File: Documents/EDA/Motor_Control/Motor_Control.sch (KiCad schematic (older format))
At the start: 7 parts

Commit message: PCB first pass
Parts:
- removed U?: ESP32-WROOM-32, RF_Module:ESP32-WROOM-32, symbol RF_Module:ESP32-WROOM-32
- added A3: Adafruit_Feather_HUZZAH32_ESP32, Module:Adafruit_Feather, symbol MCU_Module:Adafruit_Feather_HUZZAH32_ESP32
- added J1: V_MOTOR, TerminalBlock_Phoenix:TerminalBlock_Phoenix_MKDS-1,5-2_1x02_P5.00mm_Horizontal, symbol Connector:Screw_Terminal_01x02
- A1: renamed from A?; value Pololu_Breakout_DRV8825 -> R Motor Driver
- A2: renamed from A?; value Pololu_Breakout_DRV8825 -> Z Motor Driver
- C1, C2: renamed from C?; value CP -> 100u; footprint (none) -> Capacitor_THT:CP_Radial_D8.0mm_P3.50mm; symbol Device:CP -> Motor_Control-rescue:CP-Device
- M1: renamed from M?; value Stepper_Motor_bipolar -> R; footprint (none) -> Connector_PinSocket_2.54mm:PinSocket_1x04_P2.54mm_Vertical
- M2: renamed from M?; value Stepper_Motor_bipolar -> Z; footprint (none) -> Connector_PinSocket_2.54mm:PinSocket_1x04_P2.54mm_Vertical
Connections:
- net labels added: GNDD
- wire segments 68 -> 70
- no-connect marks 4 -> 25
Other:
- moved on the sheet: A1, A2, M1, M2

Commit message: libs and pcb and bom
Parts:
- removed A3: Adafruit_Feather_HUZZAH32_ESP32, Module:Adafruit_Feather, symbol MCU_Module:Adafruit_Feather_HUZZAH32_ESP32
- added J2: Barrel_Jack, Connector_BarrelJack:BarrelJack_Horizontal, symbol Connector:Barrel_Jack
- added U1: ESP32-DEVKITC-32D, MODULE_ESP32-DEVKITC-32D:MODULE_ESP32-DEVKITC-32D, symbol ESP32-DEVKITC-32D:ESP32-DEVKITC-32D
- M1, M2: footprint Connector_PinSocket_2.54mm:PinSocket_1x04_P2.54mm_Vertical -> (none)
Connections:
- net +3V3: now also U1.1 (3V3)
- net +VDC: now also J2.1
- net GND: now also J2.2
- net GNDD: now also U1.14 (GND1), U1.20 (GND3), U1.26 (GND2)
- net R_DIR: now also U1.28 (IO18)
- net R_STEP: now also U1.27 (IO19)
- net Z_DIR: now also U1.22 (IO22)
- net Z_STEP: now also U1.21 (IO23)
- no-connect marks 25 -> 4
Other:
- moved on the sheet: A1, A2, C1, C2, J1, M1, M2

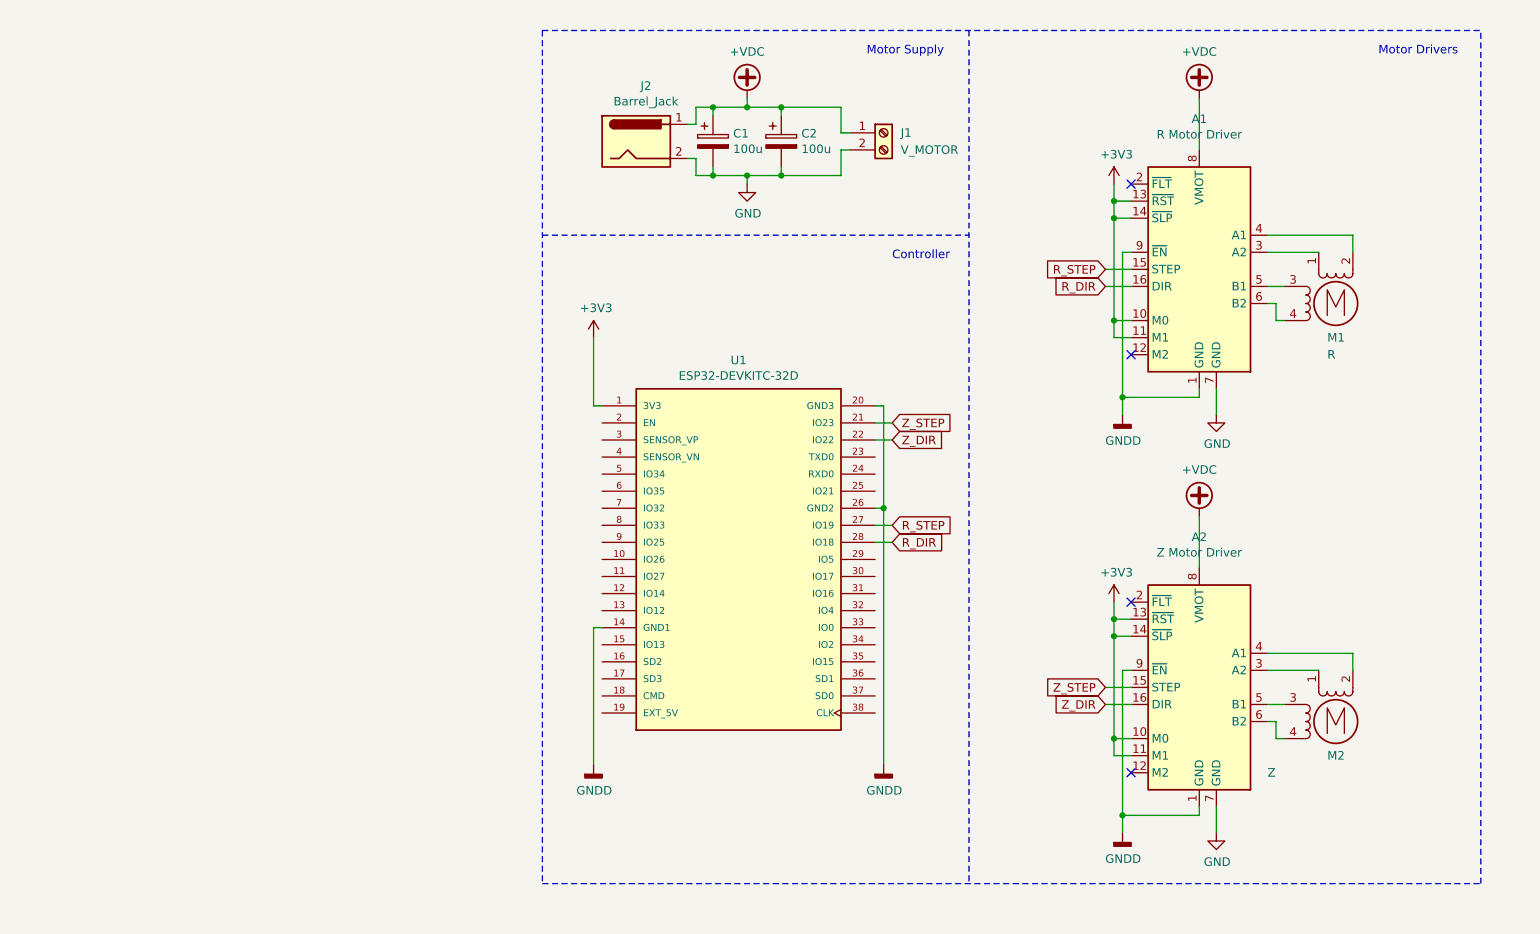
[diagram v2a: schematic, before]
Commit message: connectors placed
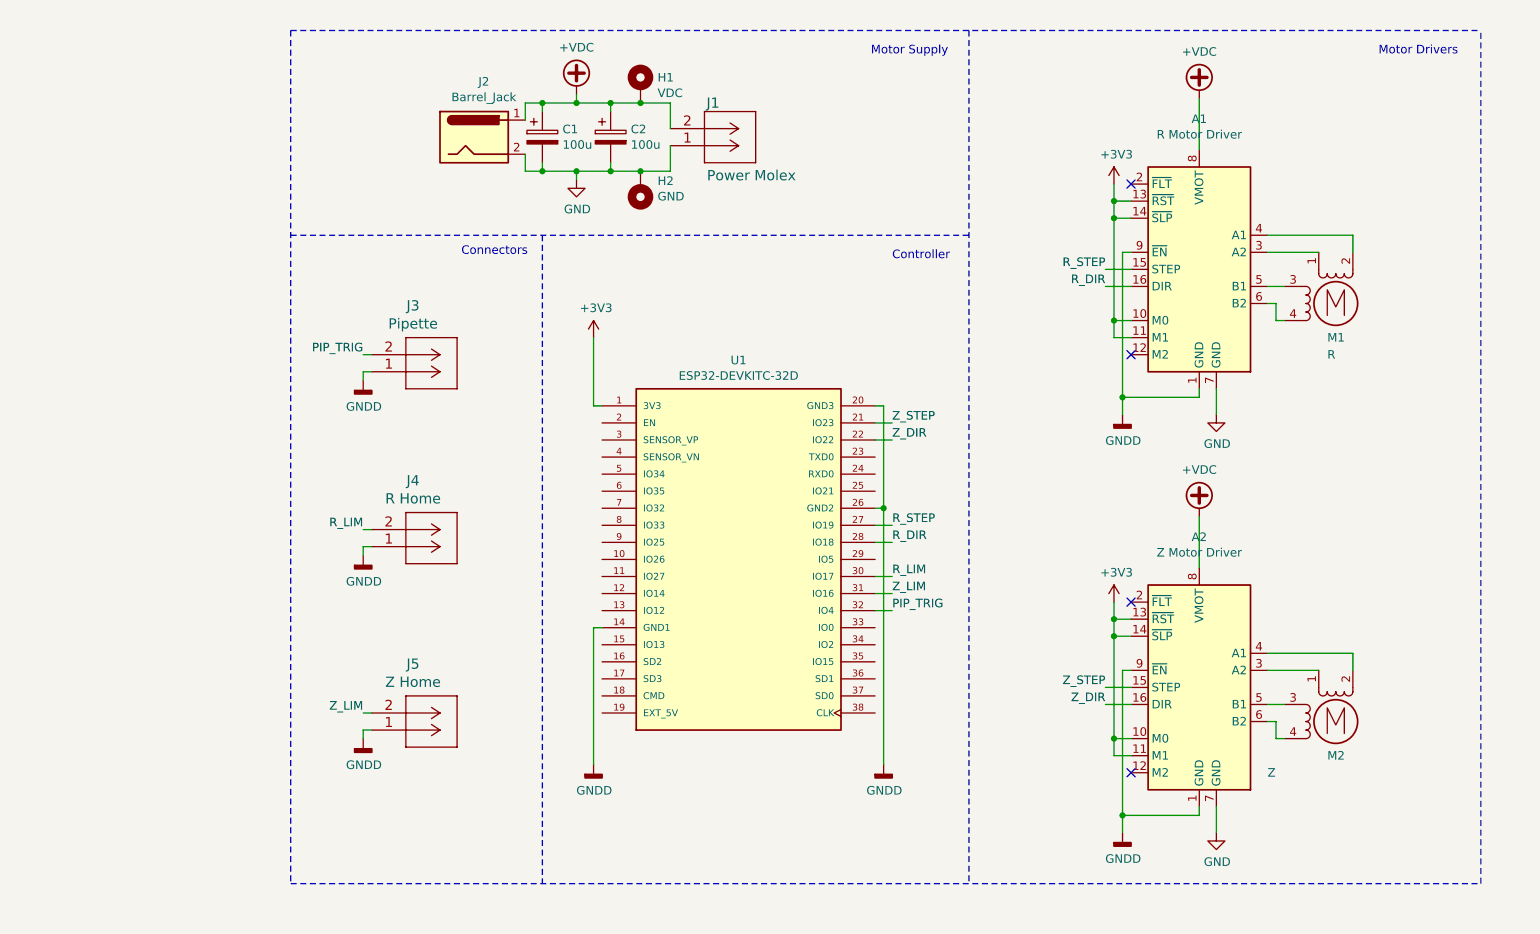
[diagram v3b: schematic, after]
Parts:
- removed J1: V_MOTOR, TerminalBlock_Phoenix:TerminalBlock_Phoenix_MKDS-1,5-2_1x02_P5.00mm_Horizontal, symbol Connector:Screw_Terminal_01x02
- added H1: VDC, MountingHole:MountingHole_3.2mm_M3_Pad_Via, symbol Mechanical:MountingHole_Pad
- added H2: GND, MountingHole:MountingHole_3.2mm_M3_Pad_Via, symbol Mechanical:MountingHole_Pad
- added J1: Power Molex, molex_sherlock:molex_sherlock_vrthdr_2pin, symbol molex_sherlock_vrthdr_2pin:353620250
- added J3: Pipette, molex_sherlock:molex_sherlock_vrthdr_2pin, symbol molex_sherlock_vrthdr_2pin:353620250
- added J4: R Home, molex_sherlock:molex_sherlock_vrthdr_2pin, symbol molex_sherlock_vrthdr_2pin:353620250
- added J5: Z Home, molex_sherlock:molex_sherlock_vrthdr_2pin, symbol molex_sherlock_vrthdr_2pin:353620250
- M1, M2: footprint (none) -> molex_sherlock:molex_sherlock_vrthdr_4pin
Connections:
- net +VDC: now also H1.1, J1.2
- net GND: now also H2.1, J1.1
- net GNDD: now also J3.1, J4.1, J5.1
- net R_LIM: now reaches U1.30 (IO17)
- net R_LIM: now also J4.2
- net Z_LIM: now reaches U1.31 (IO16)
- net Z_LIM: now also J5.2
- net PIP_TRIG: now reaches U1.32 (IO4)
- net PIP_TRIG: now also J3.2
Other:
- note added: "Connectors\n"
- moved on the sheet: C1, C2, J2

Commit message: Final pcb and bom
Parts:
- added H3, H4, H5, H6: øM3, MountingHole:MountingHole_3.2mm_M3_Pad_Via, symbol Mechanical:MountingHole_Pad
- added J6: EXP, Connector_PinHeader_2.54mm:PinHeader_2x05_P2.54mm_Vertical, symbol Connector_Generic:Conn_02x05_Odd_Even
- added TP1: Z_STEP, TestPoint:TestPoint_Pad_D1.0mm, symbol Connector:TestPoint_Small
- added TP2: Z_DIR, TestPoint:TestPoint_Pad_D1.0mm, symbol Connector:TestPoint_Small
- added TP3: R_STEP, TestPoint:TestPoint_Pad_D1.0mm, symbol Connector:TestPoint_Small
- added TP4: R_DIR, TestPoint:TestPoint_Pad_D1.0mm, symbol Connector:TestPoint_Small
- added TP5: PIP_TRIG, TestPoint:TestPoint_Pad_D1.0mm, symbol Connector:TestPoint_Small
- added TP6: Z_LIM, TestPoint:TestPoint_Pad_D1.0mm, symbol Connector:TestPoint_Small
- added TP7: R_LIM, TestPoint:TestPoint_Pad_D1.0mm, symbol Connector:TestPoint_Small
- H1: value VDC -> +VDC; footprint MountingHole:MountingHole_3.2mm_M3_Pad_Via -> MountingHole:MountingHole_3.7mm_Pad_Via
- H2: footprint MountingHole:MountingHole_3.2mm_M3_Pad_Via -> MountingHole:MountingHole_3.7mm_Pad_Via
- J1: value Power Molex -> - Power +
- J2: cost (none) -> 1.18; link (none) -> https://www.digikey.co.nz/en/products/detail/cui-devices/PJ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; man part # (none) -> PJ-002BH
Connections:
- net +3V3: now also J6.1 (Pin_1)
- net GND: now also H3.1, H4.1, H5.1, H6.1
- net GNDD: now also J6.2 (Pin_2)
- net PIP_TRIG: now also TP5.1
- net R_DIR: now also U1.27 (IO19), TP4.1; no longer U1.28 (IO18)
- net R_LIM: now also TP7.1
- net R_STEP: now also U1.28 (IO18), TP3.1; no longer U1.27 (IO19)
- net Z_DIR: now also U1.21 (IO23), TP2.1; no longer U1.22 (IO22)
- net Z_LIM: now also TP6.1
- net Z_STEP: now also U1.22 (IO22), TP1.1; no longer U1.21 (IO23)
- net IO26: now reaches U1.10 (IO26)
- net IO26: now also J6.4 (Pin_4)
- net IO27: now reaches U1.11 (IO27)
- net IO27: now also J6.6 (Pin_6)
- net IO14: now reaches U1.12 (IO14)
- net IO14: now also J6.7 (Pin_7)
- net IO12: now reaches U1.13 (IO12)
- net IO12: now also J6.3 (Pin_3)
- net IO13: now reaches U1.15 (IO13)
- net IO13: now also J6.5 (Pin_5)
- net IO32: now reaches U1.7 (IO32)
- net IO32: now also J6.8 (Pin_8)
- net IO33: now reaches U1.8 (IO33)
- net IO33: now also J6.10 (Pin_10)
- net IO25: now reaches U1.9 (IO25)
- net IO25: now also J6.9 (Pin_9)
- no-connect marks 4 -> 23
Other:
- note added: "Mounting\n"
- note added: "Test Points\n"
- moved on the sheet: A1, A2, C1, C2, H1, H2, J1, J2, J3, J4, J5, M1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

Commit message: ring light
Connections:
- net +3V3: now also A1.12 (M2), A2.12 (M2)
- no-connect marks 23 -> 21
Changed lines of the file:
@@
 Wire Wire Line
 	7050 4900 7000 4900
-NoConn ~ 7050 5500
 $Comp
 L power:+3V3 #PWR06
@@
 	1    0    0    -1
 $EndComp
-NoConn ~ 7050 3050
 $Comp
 L power:+3V3 #PWR05
@@
 	1    0    0    -1
 $EndComp
+Wire Wire Line
+	6950 2950 6950 3050
+Wire Wire Line
+	6950 3050 7050 3050
+Connection ~ 6950 2950
+Wire Wire Line
+	6950 5400 6950 5500
+Wire Wire Line
+	6950 5500 7050 5500
+Connection ~ 6950 5400
 $EndSCHEMATC
